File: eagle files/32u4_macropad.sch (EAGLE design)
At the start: 91 parts, among them J1 TYPE-C-31-M-12, Q1 16MHz, SW2 SWITCH-SMD-EVP-BB2A9B00

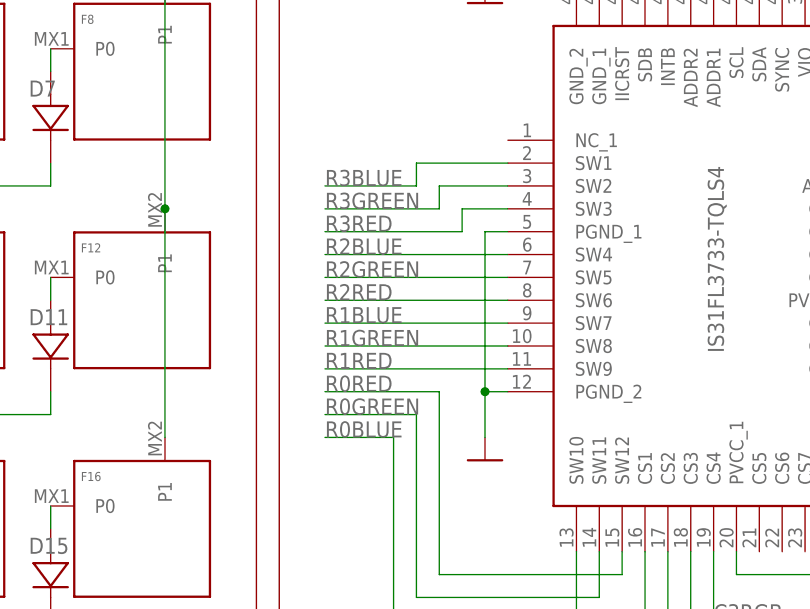
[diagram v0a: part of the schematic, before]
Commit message: Led driver connections to leds fixed in sch and brd
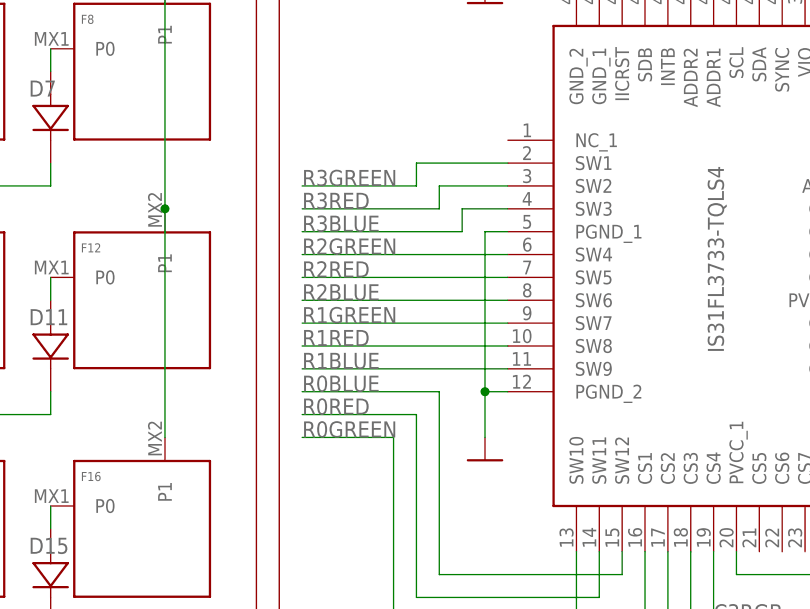
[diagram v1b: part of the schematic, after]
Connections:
- net R0BLUE: now also DRIVER.SW12; no longer DRIVER.SW10
- net R0GREEN: now also DRIVER.SW10; no longer DRIVER.SW11
- net R0RED: now also DRIVER.SW11; no longer DRIVER.SW12
- net R1BLUE: now also DRIVER.SW9; no longer DRIVER.SW7
- net R1GREEN: now also DRIVER.SW7; no longer DRIVER.SW8
- net R1RED: now also DRIVER.SW8; no longer DRIVER.SW9
- net R2BLUE: now also DRIVER.SW6; no longer DRIVER.SW4
- net R2GREEN: now also DRIVER.SW4; no longer DRIVER.SW5
- net R2RED: now also DRIVER.SW5; no longer DRIVER.SW6
- net R3BLUE: now also DRIVER.SW3; no longer DRIVER.SW1
- net R3GREEN: now also DRIVER.SW1; no longer DRIVER.SW2
- net R3RED: now also DRIVER.SW2; no longer DRIVER.SW3
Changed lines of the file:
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@@
 </segment>
 <segment>
-<pinref part="DRIVER" gate="G$1" pin="SW12"/>
-<wire x1="-58.42" y1="-101.6" x2="-58.42" y2="-104.14" width="0.1524" layer="91"/>
-<wire x1="-58.42" y1="-104.14" x2="-78.74" y2="-104.14" width="0.1524" layer="91"/>
-<wire x1="-78.74" y1="-104.14" x2="-78.74" y2="-83.82" width="0.1524" layer="91"/>
-<wire x1="-78.74" y1="-83.82" x2="-91.44" y2="-83.82" width="0.1524" layer="91"/>
-<label x="-91.44" y="-83.82" size="1.778" layer="95"/>
+<pinref part="DRIVER" gate="G$1" pin="SW11"/>
+<wire x1="-60.96" y1="-101.6" x2="-60.96" y2="-106.68" width="0.1524" layer="91"/>
+<wire x1="-60.96" y1="-106.68" x2="-81.28" y2="-106.68" width="0.1524" layer="91"/>
+<wire x1="-81.28" y1="-106.68" x2="-81.28" y2="-86.36" width="0.1524" layer="91"/>
+<wire x1="-81.28" y1="-86.36" x2="-93.98" y2="-86.36" width="0.1524" layer="91"/>
+<label x="-93.98" y="-86.36" size="1.778" layer="95"/>
 </segment>
 </net>
@@
 </segment>
 <segment>
-<pinref part="DRIVER" gate="G$1" pin="SW11"/>
-<wire x1="-60.96" y1="-101.6" x2="-60.96" y2="-106.68" width="0.1524" layer="91"/>
-<wire x1="-60.96" y1="-106.68" x2="-81.28" y2="-106.68" width="0.1524" layer="91"/>
-<wire x1="-81.28" y1="-106.68" x2="-81.28" y2="-86.36" width="0.1524" layer="91"/>
-<wire x1="-81.28" y1="-86.36" x2="-91.44" y2="-86.36" width="0.1524" layer="91"/>
-<label x="-91.44" y="-86.36" size="1.778" layer="95"/>
+<pinref part="DRIVER" gate="G$1" pin="SW10"/>
+<wire x1="-63.5" y1="-101.6" x2="-63.5" y2="-109.22" width="0.1524" layer="91"/>
+<wire x1="-63.5" y1="-109.22" x2="-83.82" y2="-109.22" width="0.1524" layer="91"/>
+<wire x1="-83.82" y1="-109.22" x2="-83.82" y2="-88.9" width="0.1524" layer="91"/>
+<wire x1="-83.82" y1="-88.9" x2="-93.98" y2="-88.9" width="0.1524" layer="91"/>
+<label x="-93.98" y="-88.9" size="1.778" layer="95"/>
 </segment>
 </net>
@@
 </segment>
 <segment>
-<pinref part="DRIVER" gate="G$1" pin="SW10"/>
-<wire x1="-63.5" y1="-101.6" x2="-63.5" y2="-109.22" width="0.1524" layer="91"/>
-<wire x1="-63.5" y1="-109.22" x2="-83.82" y2="-109.22" width="0.1524" layer="91"/>
-<wire x1="-83.82" y1="-109.22" x2="-83.82" y2="-88.9" width="0.1524" layer="91"/>
-<wire x1="-83.82" y1="-88.9" x2="-91.44" y2="-88.9" width="0.1524" layer="91"/>
-<label x="-91.44" y="-88.9" size="1.778" layer="95"/>
+<pinref part="DRIVER" gate="G$1" pin="SW12"/>
+<wire x1="-58.42" y1="-101.6" x2="-58.42" y2="-104.14" width="0.1524" layer="91"/>
+<wire x1="-58.42" y1="-104.14" x2="-78.74" y2="-104.14" width="0.1524" layer="91"/>
+<wire x1="-78.74" y1="-104.14" x2="-78.74" y2="-83.82" width="0.1524" layer="91"/>
+<wire x1="-78.74" y1="-83.82" x2="-93.98" y2="-83.82" width="0.1524" layer="91"/>
+<label x="-93.98" y="-83.82" size="1.778" layer="95"/>
 </segment>
 </net>
@@
 </net>
 <net name="R1RED" class="0">
-<segment>
-<pinref part="DRIVER" gate="G$1" pin="SW9"/>
-<wire x1="-71.12" y1="-81.28" x2="-91.44" y2="-81.28" width="0.1524" layer="91"/>
-<label x="-91.44" y="-81.28" size="1.778" layer="95"/>
-</segment>
 <segment>
 <wire x1="109.22" y1="-40.64" x2="104.14" y2="-40.64" width="0.1524" layer="91"/>
@@
 <pinref part="RGB8" gate="G$1" pin="R"/>
 </segment>
+<segment>
+<pinref part="DRIVER" gate="G$1" pin="SW8"/>
+<wire x1="-71.12" y1="-78.74" x2="-93.98" y2="-78.74" width="0.1524" layer="91"/>
+<label x="-93.98" y="-78.74" size="1.778" layer="95"/>
+</segment>
 </net>
 <net name="R1GREEN" class="0">
-<segment>
-<pinref part="DRIVER" gate="G$1" pin="SW8"/>
-<wire x1="-71.12" y1="-78.74" x2="-91.44" y2="-78.74" width="0.1524" layer="91"/>
-<label x="-91.44" y="-78.74" size="1.778" layer="95"/>
-</segment>
 <segment>
 <wire x1="109.22" y1="-43.18" x2="106.68" y2="-43.18" width="0.1524" layer="91"/>
@@
 <pinref part="RGB8" gate="G$1" pin="G"/>
 </segment>
+<segment>
+<pinref part="DRIVER" gate="G$1" pin="SW7"/>
+<wire x1="-71.12" y1="-76.2" x2="-93.98" y2="-76.2" width="0.1524" layer="91"/>
+<label x="-93.98" y="-76.2" size="1.778" layer="95"/>
+</segment>
 </net>
 <net name="R1BLUE" class="0">
-<segment>
-<pinref part="DRIVER" gate="G$1" pin="SW7"/>
-<wire x1="-71.12" y1="-76.2" x2="-91.44" y2="-76.2" width="0.1524" layer="91"/>
-<label x="-91.44" y="-76.2" size="1.778" layer="95"/>
-</segment>
 <segment>
 <wire x1="81.28" y1="-45.72" x2="81.28" y2="-55.88" width="0.1524" layer="91"/>
@@
 <pinref part="RGB8" gate="G$1" pin="B"/>
 </segment>
+<segment>
+<pinref part="DRIVER" gate="G$1" pin="SW9"/>
+<wire x1="-71.12" y1="-81.28" x2="-93.98" y2="-81.28" width="0.1524" layer="91"/>
+<label x="-93.98" y="-81.28" size="1.778" layer="95"/>
+</segment>
 </net>
 <net name="C0SWTCH" class="0">
@@
 </net>
 <net name="R2RED" class="0">
-<segment>
-<pinref part="DRIVER" gate="G$1" pin="SW6"/>
-<wire x1="-71.12" y1="-73.66" x2="-91.44" y2="-73.66" width="0.1524" layer="91"/>
-<label x="-91.44" y="-73.66" size="1.778" layer="95"/>
-</segment>
 <segment>
 <wire x1="109.22" y1="-60.96" x2="104.14" y2="-60.96" width="0.1524" layer="91"/>
@@
 <pinref part="RGB12" gate="G$1" pin="R"/>
 </segment>
+<segment>
+<pinref part="DRIVER" gate="G$1" pin="SW5"/>
+<wire x1="-71.12" y1="-71.12" x2="-93.98" y2="-71.12" width="0.1524" layer="91"/>
+<label x="-93.98" y="-71.12" size="1.778" layer="95"/>
+</segment>
 </net>
 <net name="R2GREEN" class="0">
-<segment>
-<pinref part="DRIVER" gate="G$1" pin="SW5"/>
-<wire x1="-71.12" y1="-71.12" x2="-91.44" y2="-71.12" width="0.1524" layer="91"/>
-<label x="-91.44" y="-71.12" size="1.778" layer="95"/>
-</segment>
 <segment>
 <wire x1="81.28" y1="-63.5" x2="78.74" y2="-63.5" width="0.1524" layer="91"/>
@@
 <pinref part="RGB12" gate="G$1" pin="G"/>
 </segment>
+<segment>
+<pinref part="DRIVER" gate="G$1" pin="SW4"/>
+<wire x1="-71.12" y1="-68.58" x2="-93.98" y2="-68.58" width="0.1524" layer="91"/>
+<label x="-93.98" y="-68.58" size="1.778" layer="95"/>
+</segment>
 </net>
 <net name="R2BLUE" class="0">
-<segment>
-<pinref part="DRIVER" gate="G$1" pin="SW4"/>
-<wire x1="-71.12" y1="-68.58" x2="-91.44" y2="-68.58" width="0.1524" layer="91"/>
-<label x="-91.44" y="-68.58" size="1.778" layer="95"/>
-</segment>
 <segment>
 <wire x1="109.22" y1="-66.04" x2="109.22" y2="-76.2" width="0.1524" layer="91"/>
@@
 <pinref part="RGB11" gate="G$1" pin="B"/>
 <pinref part="RGB12" gate="G$1" pin="B"/>
+</segment>
+<segment>
+<pinref part="DRIVER" gate="G$1" pin="SW6"/>
+<wire x1="-71.12" y1="-73.66" x2="-93.98" y2="-73.66" width="0.1524" layer="91"/>
+<label x="-93.98" y="-73.66" size="1.778" layer="95"/>
 </segment>
 </net>
@@
 </segment>
 <segment>
-<pinref part="DRIVER" gate="G$1" pin="SW3"/>
-<wire x1="-71.12" y1="-63.5" x2="-76.2" y2="-63.5" width="0.1524" layer="91"/>
-<wire x1="-76.2" y1="-63.5" x2="-76.2" y2="-66.04" width="0.1524" layer="91"/>
-<wire x1="-76.2" y1="-66.04" x2="-91.44" y2="-66.04" width="0.1524" layer="91"/>
-<label x="-91.44" y="-66.04" size="1.778" layer="95"/>
+<pinref part="DRIVER" gate="G$1" pin="SW2"/>
+<wire x1="-71.12" y1="-60.96" x2="-78.74" y2="-60.96" width="0.1524" layer="91"/>
+<wire x1="-78.74" y1="-60.96" x2="-78.74" y2="-63.5" width="0.1524" layer="91"/>
+<wire x1="-78.74" y1="-63.5" x2="-93.98" y2="-63.5" width="0.1524" layer="91"/>
+<label x="-93.98" y="-63.5" size="1.778" layer="95"/>
 </segment>
 </net>
@@
 </segment>
 <segment>
-<pinref part="DRIVER" gate="G$1" pin="SW2"/>
-<wire x1="-71.12" y1="-60.96" x2="-78.74" y2="-60.96" width="0.1524" layer="91"/>
-<wire x1="-78.74" y1="-60.96" x2="-78.74" y2="-63.5" width="0.1524" layer="91"/>
-<wire x1="-78.74" y1="-63.5" x2="-91.44" y2="-63.5" width="0.1524" layer="91"/>
-<label x="-91.44" y="-63.5" size="1.778" layer="95"/>
+<pinref part="DRIVER" gate="G$1" pin="SW1"/>
+<wire x1="-71.12" y1="-58.42" x2="-81.28" y2="-58.42" width="0.1524" layer="91"/>
+<wire x1="-81.28" y1="-58.42" x2="-81.28" y2="-60.96" width="0.1524" layer="91"/>
+<wire x1="-81.28" y1="-60.96" x2="-93.98" y2="-60.96" width="0.1524" layer="91"/>
+<label x="-93.98" y="-60.96" size="1.778" layer="95"/>
 </segment>
 </net>
@@
 </segment>
 <segment>
-<pinref part="DRIVER" gate="G$1" pin="SW1"/>
-<wire x1="-71.12" y1="-58.42" x2="-81.28" y2="-58.42" width="0.1524" layer="91"/>
-<wire x1="-81.28" y1="-58.42" x2="-81.28" y2="-60.96" width="0.1524" layer="91"/>
-<wire x1="-81.28" y1="-60.96" x2="-91.44" y2="-60.96" width="0.1524" layer="91"/>
-<label x="-91.44" y="-60.96" size="1.778" layer="95"/>
-</segment>
-</net>
+<pinref part="DRIVER" gate="G$1" pin="SW3"/>
+<wire x1="-71.12" y1="-63.5" x2="-76.2" y2="-63.5" width="0.1524" layer="91"/>
+<wire x1="-76.2" y1="-63.5" x2="-76.2" y2="-66.04" width="0.1524" layer="91"/>
+<wire x1="-76.2" y1="-66.04" x2="-93.98" y2="-66.04" width="0.1524" layer="91"/>
+<label x="-93.98" y="-66.04" size="1.778" layer="95"/>
+</segment>
+</net>

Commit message: brd minor fixes
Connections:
- net R1SWTCH: now also MCU.PD6(T1/ADC9/!OC4D); no longer MCU.PB7(PCINT7/OC0A/OC1C/!RTS)
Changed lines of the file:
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@@
 </segment>
 <segment>
-<pinref part="MCU" gate="G$1" pin="PB7(PCINT7/OC0A/OC1C/!RTS)"/>
-<wire x1="-30.48" y1="12.7" x2="-17.78" y2="12.7" width="0.1524" layer="91"/>
-<label x="-17.78" y="12.7" size="1.778" layer="95"/>
+<pinref part="MCU" gate="G$1" pin="PD6(T1/ADC9/!OC4D)"/>
+<wire x1="-30.48" y1="40.64" x2="-17.78" y2="40.64" width="0.1524" layer="91"/>
+<label x="-17.78" y="40.64" size="1.778" layer="95"/>
 </segment>
 </net>

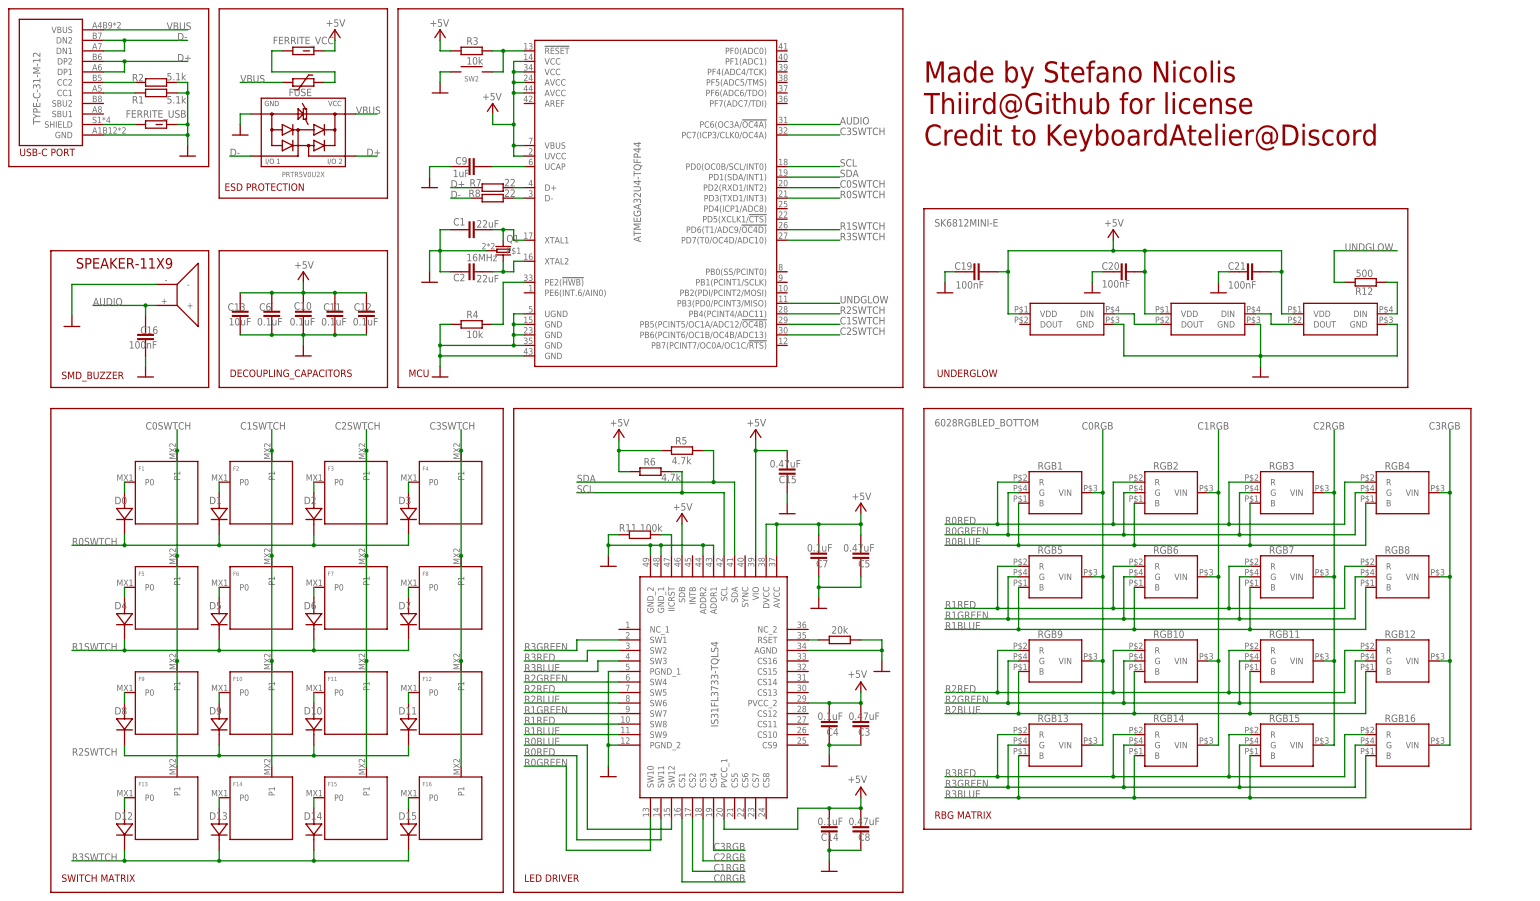
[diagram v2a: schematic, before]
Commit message: Enlarged pcb on top for case matching, re routed to accomodate this change
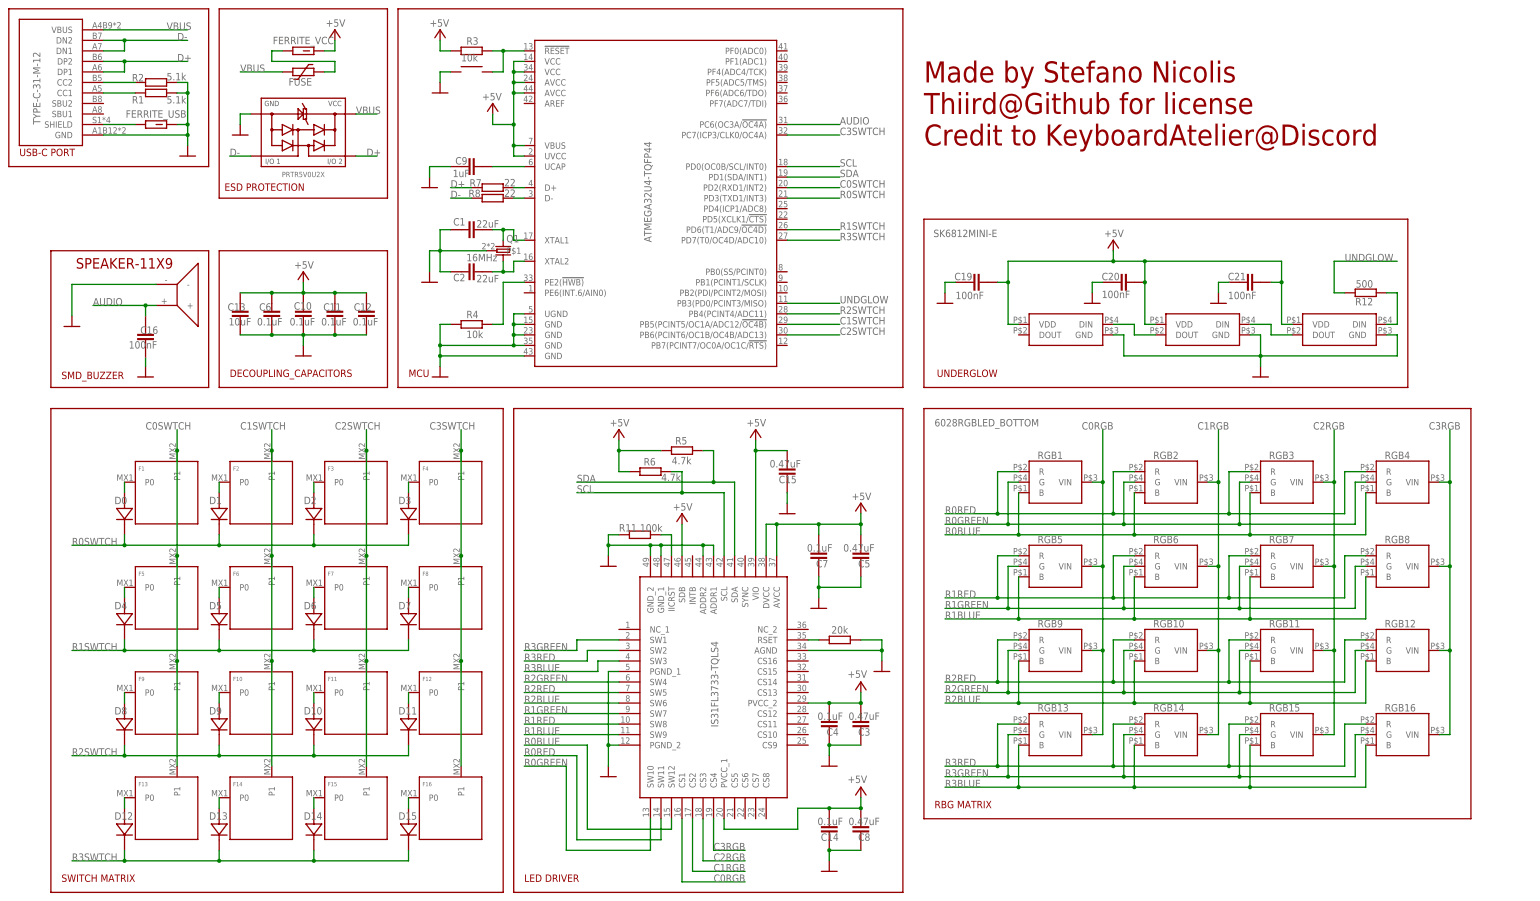
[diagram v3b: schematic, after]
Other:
- moved on the sheet: C19, C20, C21, FUSE, R12, RGB1, RGB10, RGB11, RGB12, RGB13, RGB14, RGB15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

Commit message: Fixed xtal caps value and missing C4 name on brd
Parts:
- C1, C2: value 22uF -> 22pF
- renumbered SK6812MINI-E to UGLOW3
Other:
- note removed: "Credit to KeyboardAtelier@Discord"
- note removed: "Made by Stefano Nicolis Thiird@Github for license"

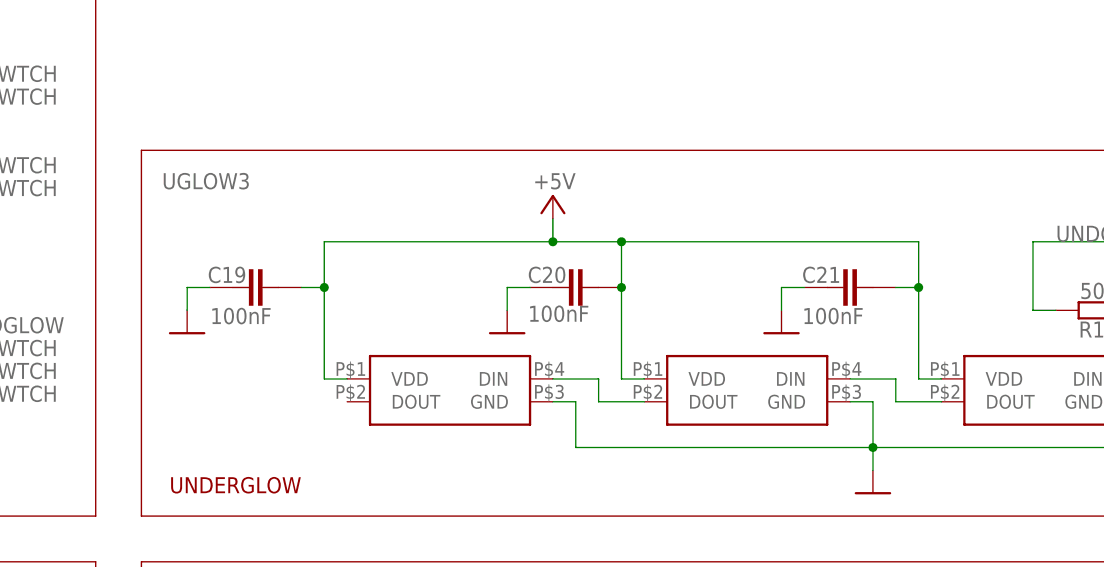
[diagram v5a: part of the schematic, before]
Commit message: Rgb matrix leds routing done, underglow leds routing done
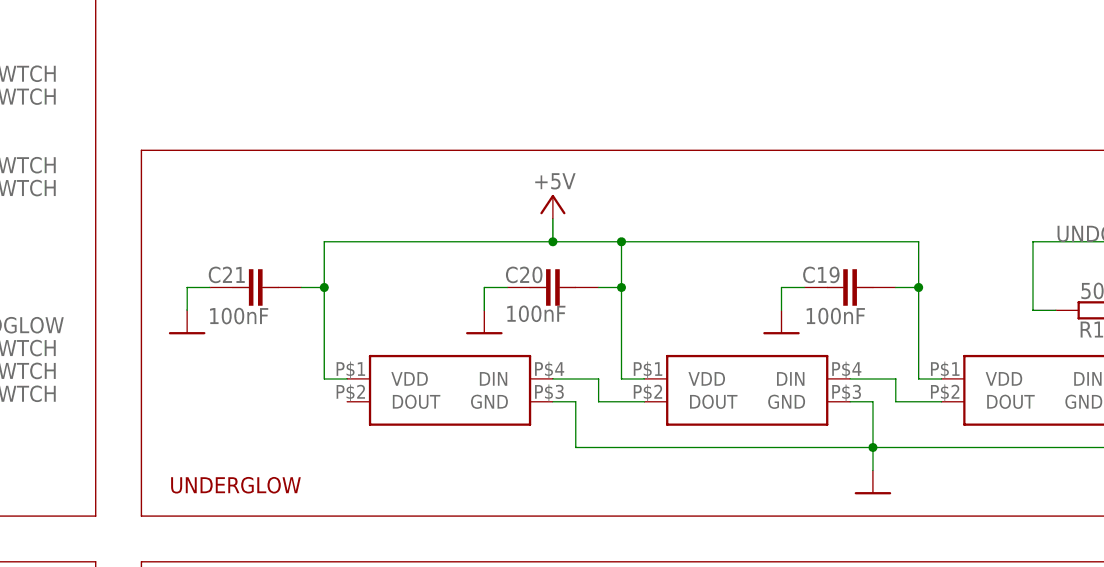
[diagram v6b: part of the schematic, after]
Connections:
- net N$25: now also UGLOW1.DIN; no longer UGLOW3.DIN
- net N$39: now also UGLOW3.DOUT; no longer UGLOW1.DOUT
- net N$7: now also UGLOW3.DIN; no longer UGLOW1.DIN
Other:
- moved on the sheet: C19, C20, C21
